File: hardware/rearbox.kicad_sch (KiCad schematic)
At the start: 21 parts, among them J1 Conn_01x06, SW1 Reset, U1 STM32G473RCTx, Y1 ABM8G-48.000MHZ

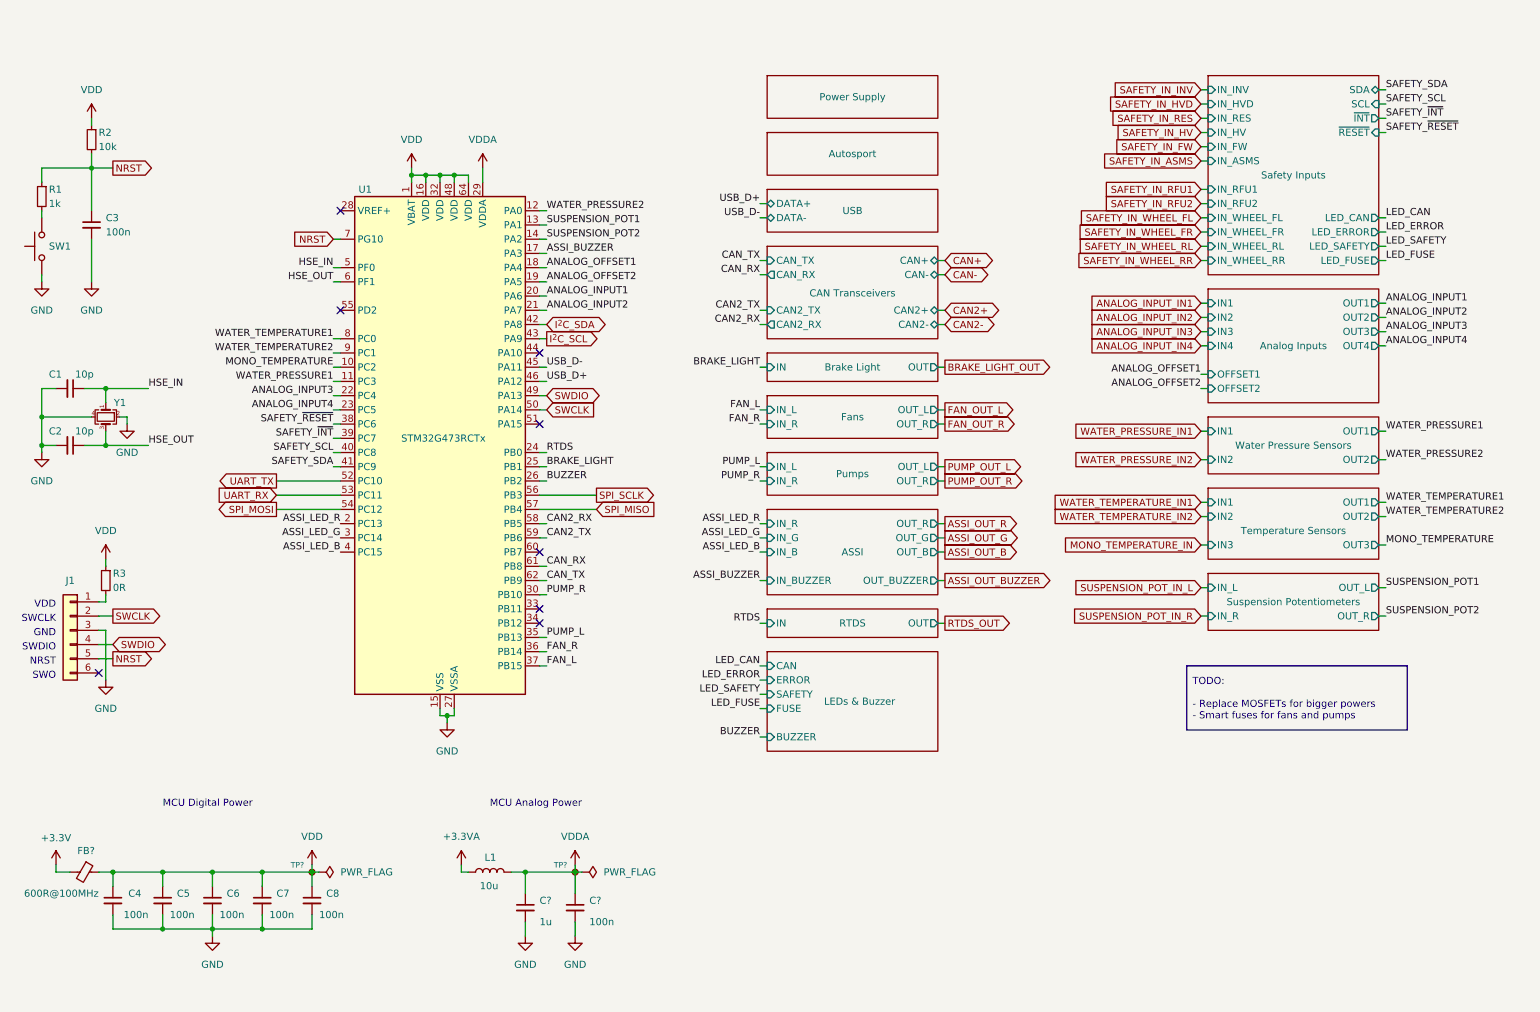
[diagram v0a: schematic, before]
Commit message: Improve the schematic according to the feedback
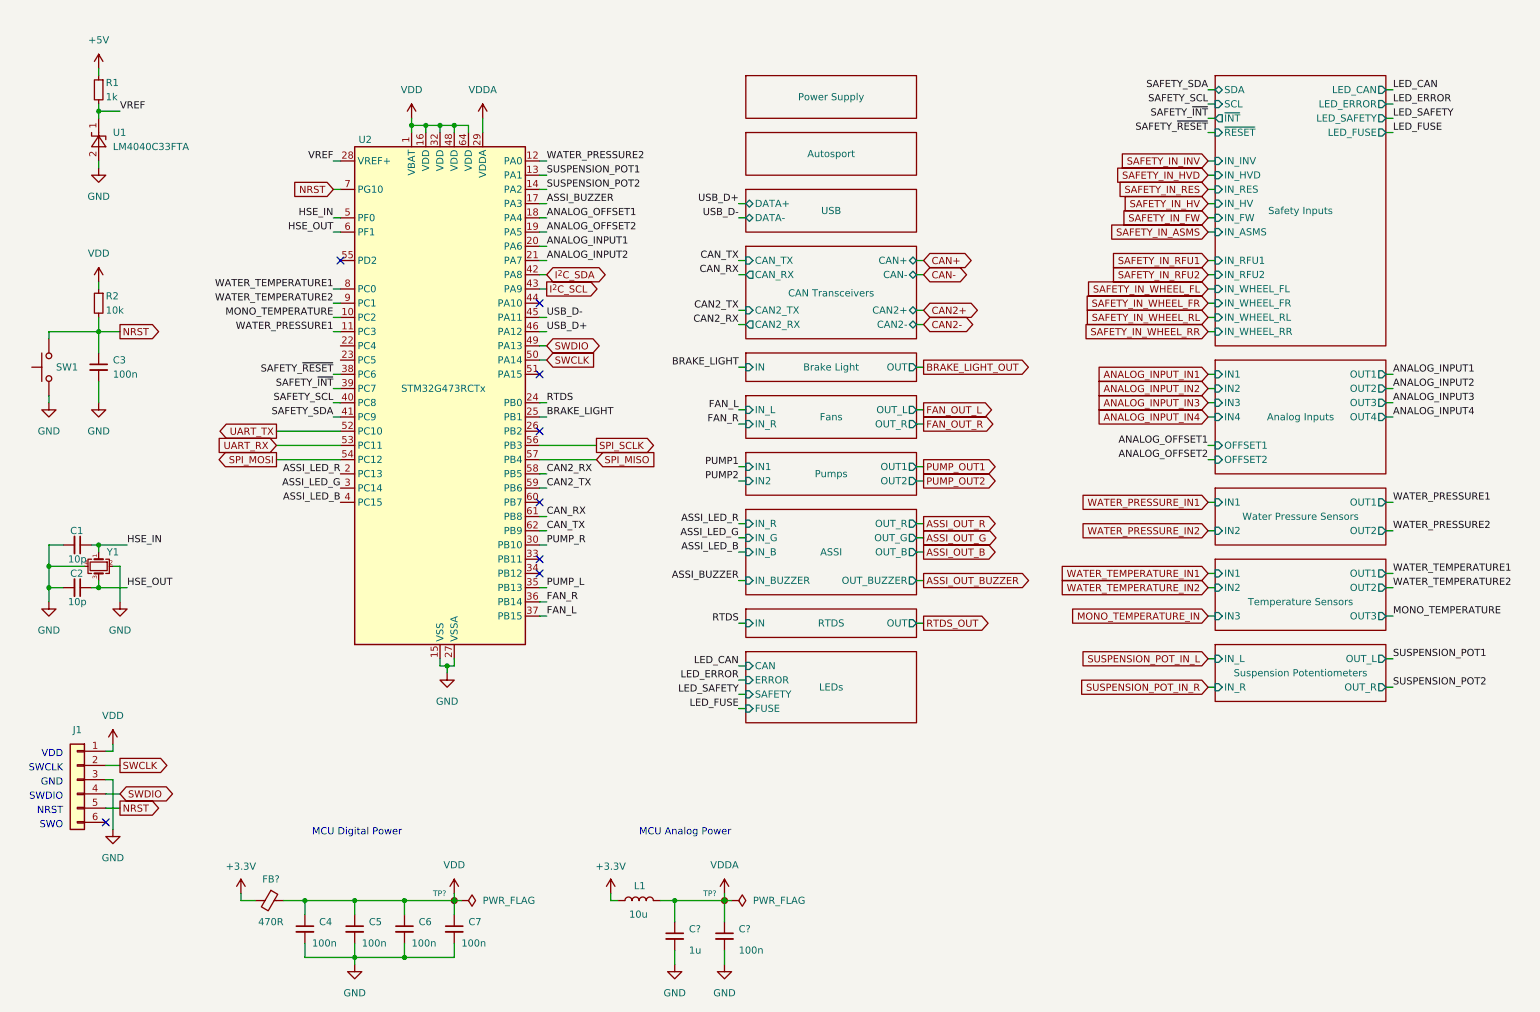
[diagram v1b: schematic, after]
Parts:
- removed C4: 100n, Capacitor_SMD:C_0603_1608Metric, symbol Device:C_Small
- removed R3: 0R, Resistor_SMD:R_0603_1608Metric, symbol Device:R_Small
- added U1: LM4040C33FTA, Package_TO_SOT_SMD:SOT-23, symbol Reference_Voltage:LM4040DBZ-3
- FB?: value 600R@100MHz -> 470R
- renumbered C5 to C4, C6 to C5, C7 to C6, C8 to C7, U1 to U2
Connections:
- net +3.3VA is gone; now on net +3.3V: L1.1
- net ANALOG_INPUT3: no longer U2.22 (PC4)
- net ANALOG_INPUT4: no longer U2.23 (PC5)
- net GND: now also U1.2 (A)
- net NRST: now also SW1.2; no longer R1.1
- net VDD: now also J1.1 (Pin_1)
- net VREF: now reaches R1.2
- net VREF: now also U2.28 (VREF+), U1.1 (K); no longer SW1.2
- net BUZZER: no longer names the net of U2.26 (PB2)
- new net +5V: R1.1
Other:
- sheet LEDs & Buzzer renamed LEDs
- sheet LEDs ports: added none; removed BUZZER
- sheet Pumps ports: added IN1, IN2, OUT1, OUT2; removed IN_L, IN_R, OUT_L, OUT_R
- moved on the sheet: C1, C2, C3, C4, C5, C6, C7, C?, FB?, J1, L1, R2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

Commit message: Add high-side drivers to the fans and pumps
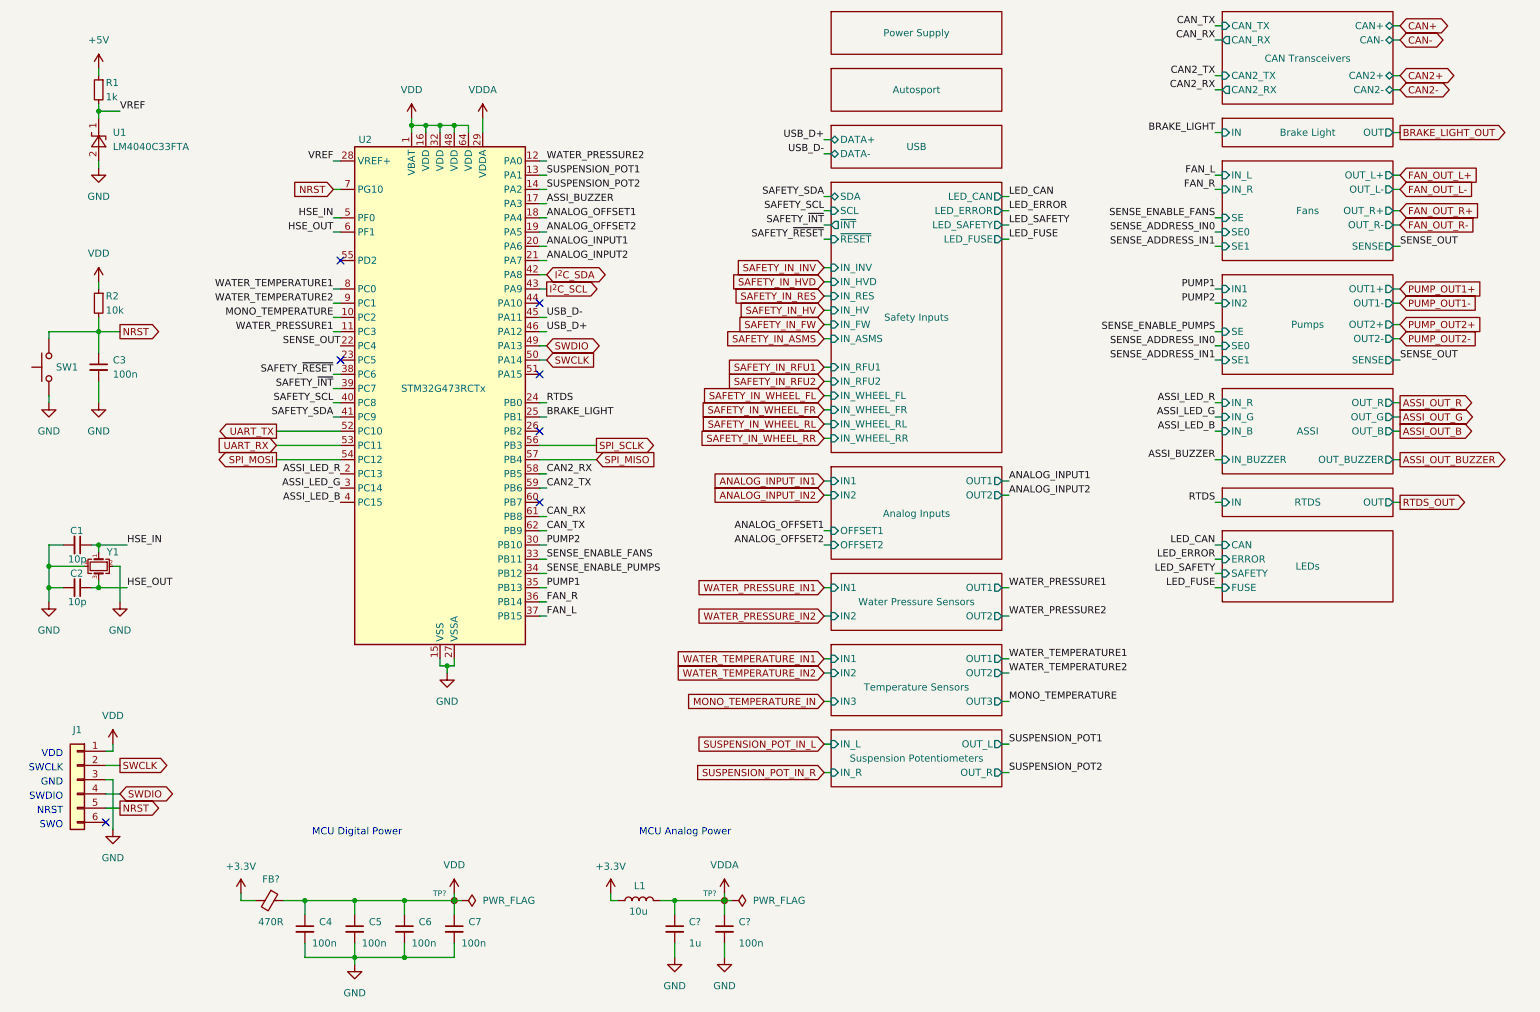
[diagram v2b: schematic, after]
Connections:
- net PUMP_L is gone; now on net PUMP1: U2.35 (PB13)
- net PUMP_R is gone; now on net PUMP2: U2.30 (PB10)
- net SENSE_OUT: now reaches U2.22 (PC4)
- net SENSE_ENABLE_FANS: now reaches U2.33 (PB11)
- net SENSE_ENABLE_PUMPS: now reaches U2.34 (PB12)
- no-connect marks 8 -> 7
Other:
- sheet Analog Inputs ports: added none; removed IN3, IN4, OUT3, OUT4
- sheet Fans ports: added OUT_L+, OUT_L-, OUT_R+, OUT_R-, SE, SE0, SE1, SENSE; removed OUT_L, OUT_R
- sheet Pumps ports: added OUT1+, OUT1-, OUT2+, OUT2-, SE, SE0, SE1, SENSE; removed OUT1, OUT2
- moved on the sheet: C?

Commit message: Improve the diagram based on the feedback
- add an input LC filter
- remove the USB connector
- add a programmer connector
- move optocouplers into a subsheet
- add a suspension tension meter IC
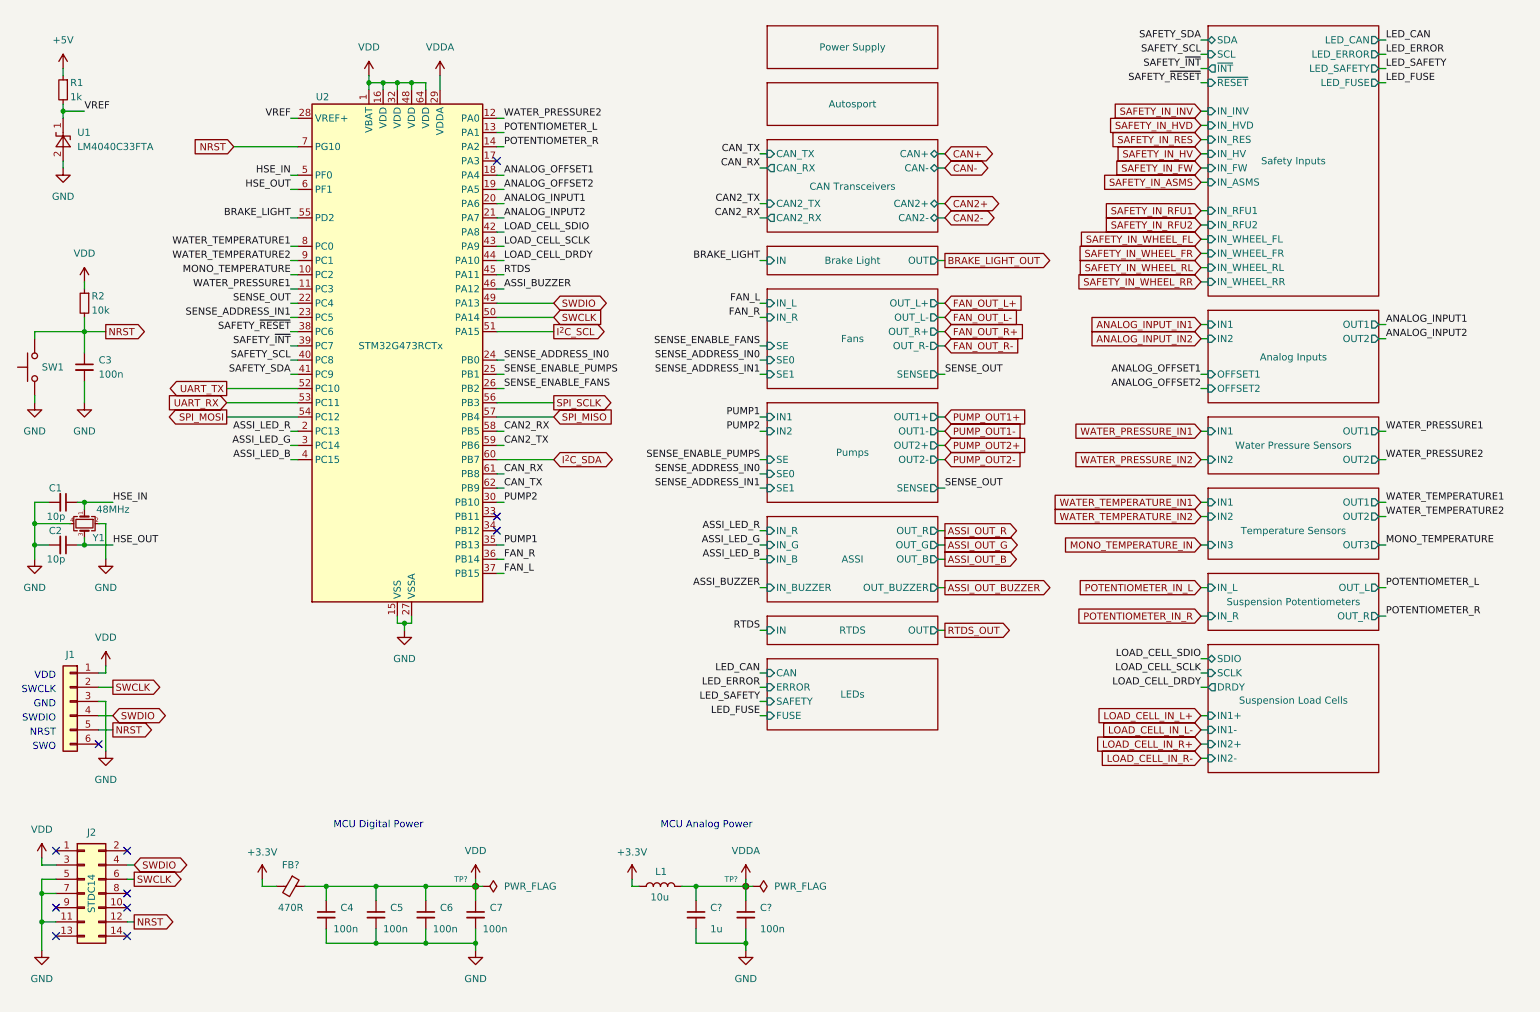
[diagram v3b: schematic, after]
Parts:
- added J2: STDC14, Connector_PinHeader_1.27mm:PinHeader_2x07_P1.27mm_Vertical_SMD, symbol Connector_Generic:Conn_02x07_Odd_Even
- J1: value Conn_01x06 -> Goldpin
- SW1: Component (none) -> B3U-1000PM
- Y1: value ABM8G-48.000MHZ -> 48MHz; Component (none) -> ABM8G-48.000MHZ
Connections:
- net USB_D+ is gone; now on net ASSI_BUZZER: U2.46 (PA12)
- net USB_D- is gone; now on net RTDS: U2.45 (PA11)
- net ASSI_BUZZER: no longer U2.17 (PA3)
- net BRAKE_LIGHT: now also U2.55 (PD2); no longer U2.25 (PB1)
- net GND: now also J2.11 (Pin_11), J2.5 (Pin_5), J2.7 (Pin_7)
- net I^{2}C_SCL: now also U2.51 (PA15); no longer U2.43 (PA9)
- net I^{2}C_SDA: now also U2.60 (PB7); no longer U2.42 (PA8)
- net NRST: now also J2.12 (Pin_12)
- net RTDS: no longer U2.24 (PB0)
- net SENSE_ADDRESS_IN0: now also U2.24 (PB0)
- net SENSE_ADDRESS_IN1: now also U2.23 (PC5)
- net SENSE_ENABLE_FANS: now also U2.26 (PB2); no longer U2.33 (PB11)
- net SENSE_ENABLE_PUMPS: now also U2.25 (PB1); no longer U2.34 (PB12)
- net SWCLK: now also J2.6 (Pin_6)
- net SWDIO: now also J2.4 (Pin_4)
- net VDD: now also J2.3 (Pin_3)
- net LOAD_CELL_DRDY: now reaches U2.44 (PA10)
- net SUSPENSION_POT1 renamed POTENTIOMETER_L
- net SUSPENSION_POT2 renamed POTENTIOMETER_R
- new net LOAD_CELL_SCLK: U2.43 (PA9)
- new net LOAD_CELL_SDIO: U2.42 (PA8)
- no-connect marks 7 -> 11
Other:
- removed sheet USB
- added sheet Suspension Load Cells (suspension_load_cells.kicad_sch)
- moved on the sheet: C1, C2, C3, C4, C5, C6, C7, C?, FB?, J1, L1, R1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
